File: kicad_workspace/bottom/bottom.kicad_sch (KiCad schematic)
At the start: 64 parts, among them J1 Battery connector, J2 Battery connector, M1 N20_MOTOR_EXTENDED_SHAFT, M2 N20_MOTOR_EXTENDED_SHAFT, U1 DRV8833PWP, U12 ACS712-5A, U13 ACS712-5A, U3 STM32F303RETx, U4 BNO055, Y1 32.768kHz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

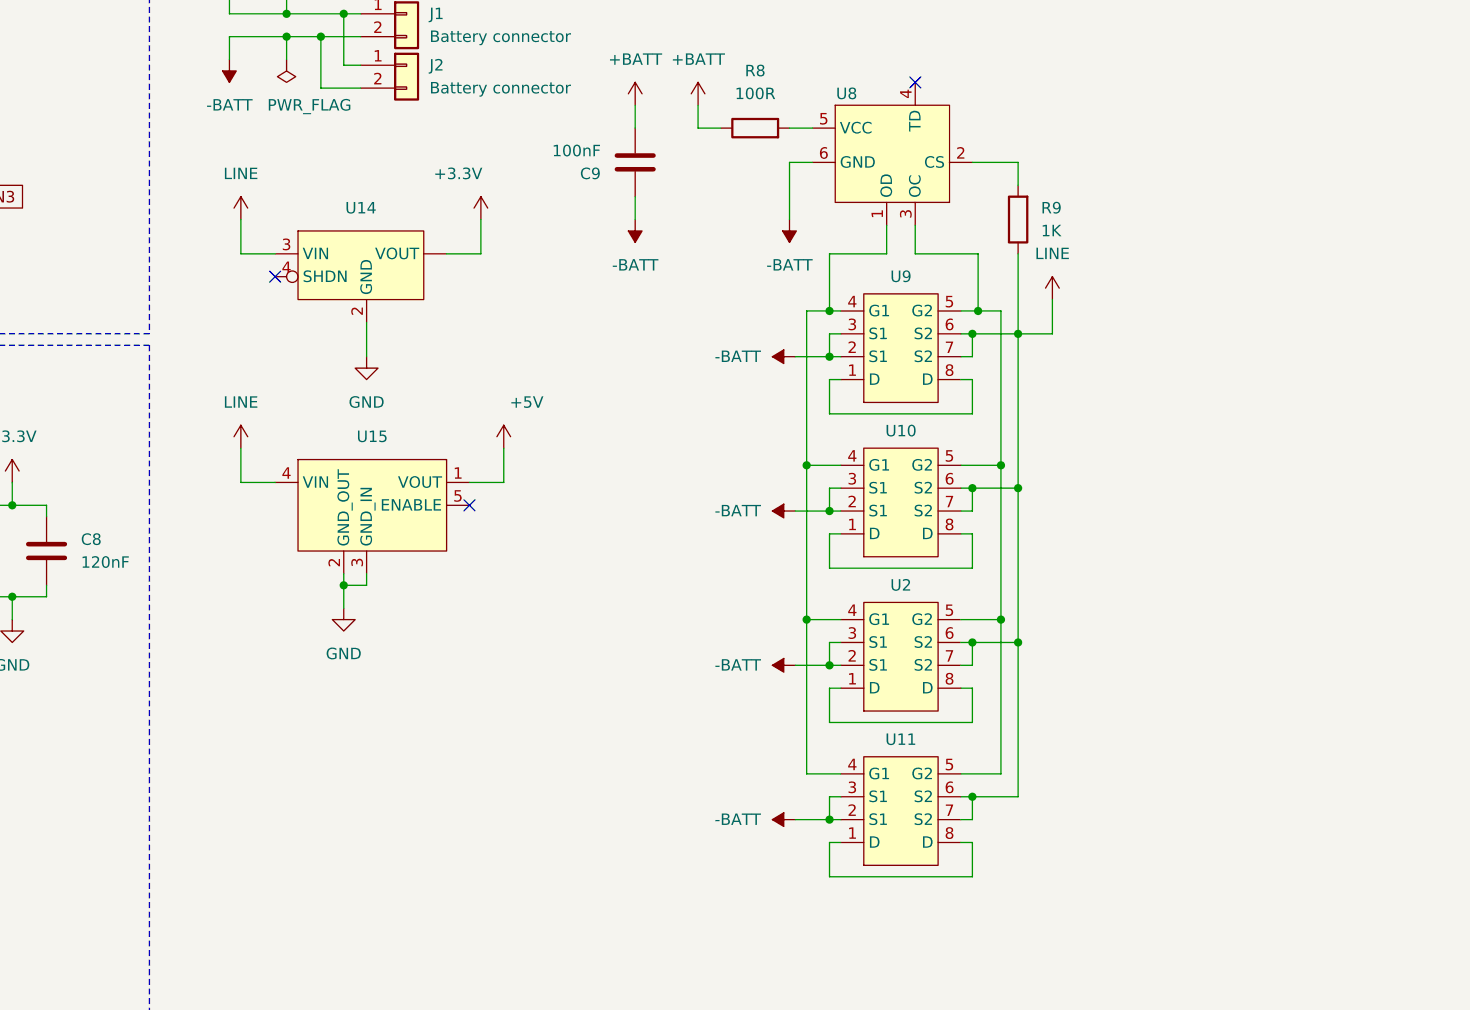
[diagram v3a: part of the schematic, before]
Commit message: add batt_prot symbol. clean schematic
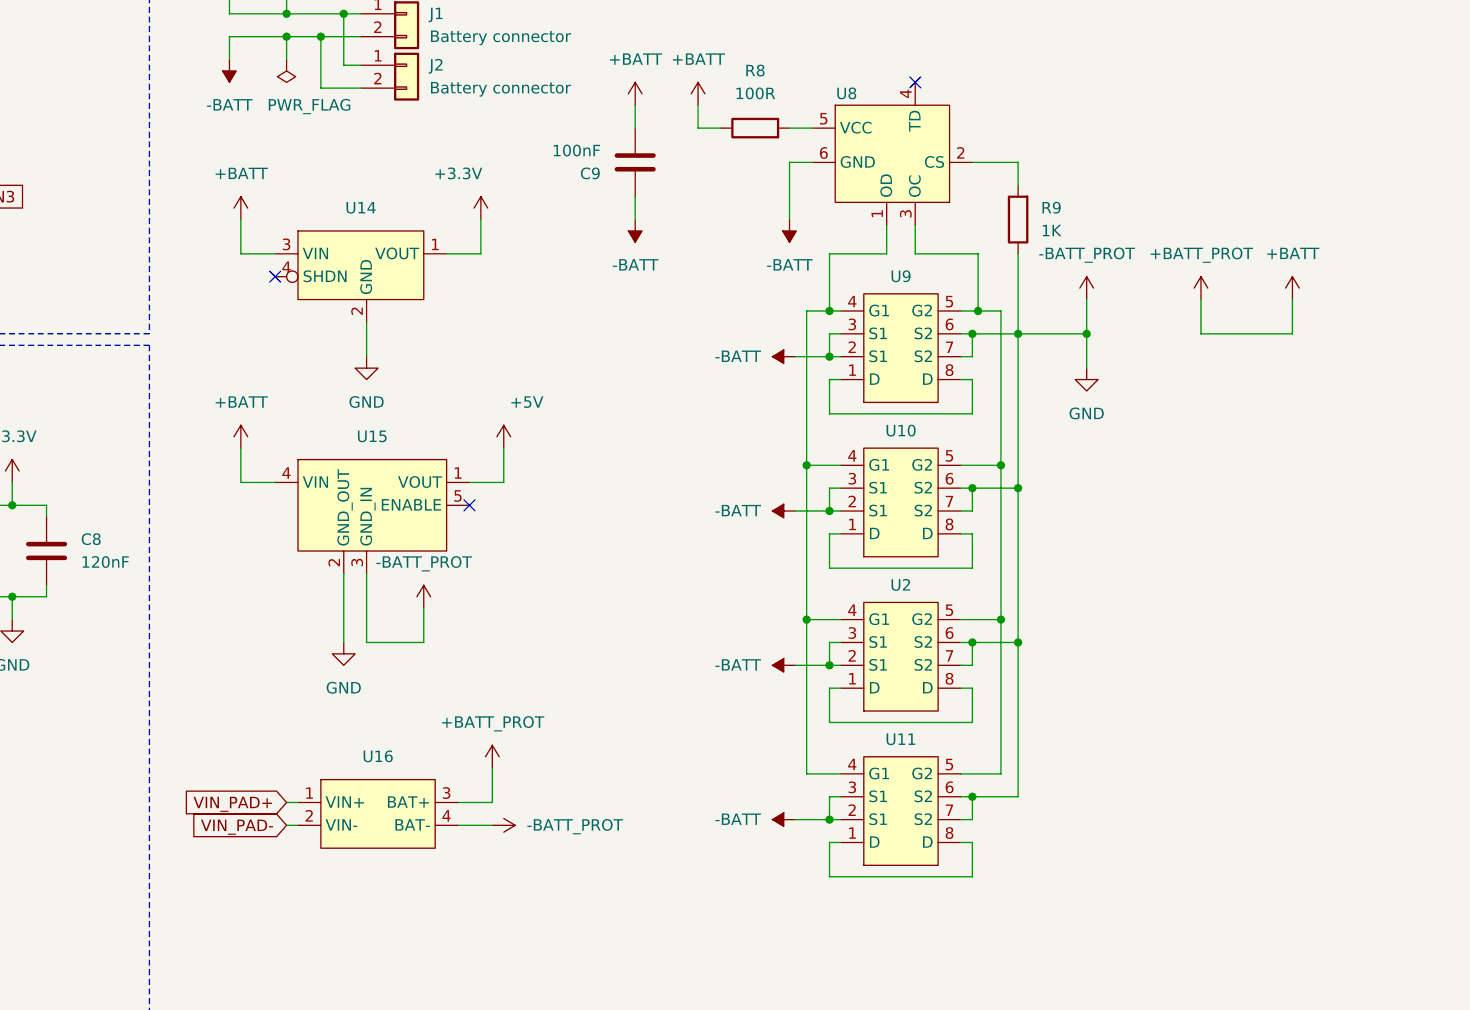
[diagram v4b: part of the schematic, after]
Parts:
- added U16: ~, pololu:TP5100, symbol pololu:TP5100
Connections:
- net +3.3V: now also U14.1 (VOUT); no longer U14. (VOUT)
- net +BATT: now also U14.3 (VIN), U15.4 (VIN), U16.3 (BAT+)
- net GND renamed -BATT_PROT
- net -BATT_PROT: now also R9.1, U10.6 (S2), U10.7 (S2), U11.6 (S2), U11.7 (S2), U2.6 (S2), U2.7 (S2), U9.6 (S2), U9.7 (S2), U16.4 (BAT-)
- removed net LINE: R9.1, U10.6 (S2), U10.7 (S2), U11.6 (S2), U11.7 (S2), U14.3 (VIN), U15.4 (VIN), U2.6 (S2), U2.7 (S2), U9.6 (S2), U9.7 (S2)
- new net VIN_PAD+: U16.1 (VIN+)
- new net VIN_PAD-: U16.2 (VIN-)

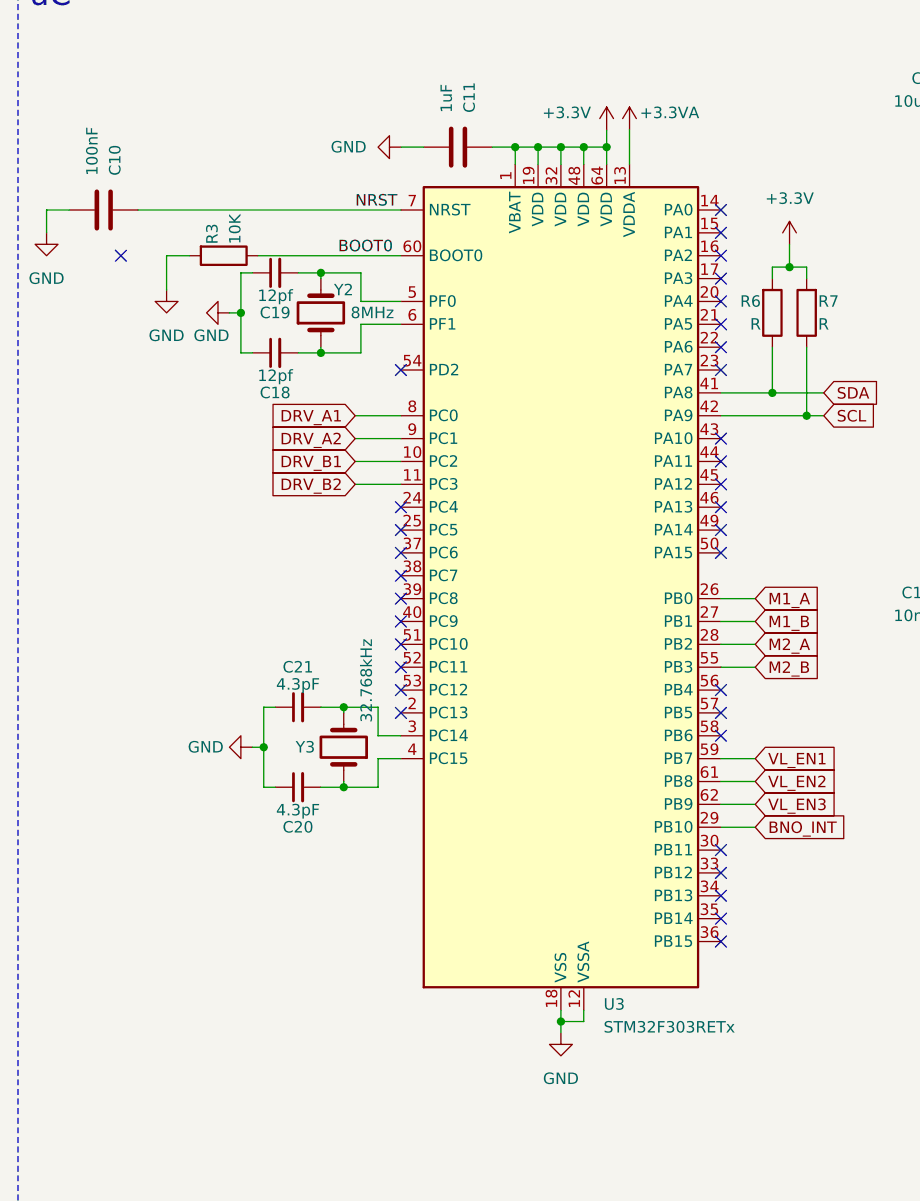
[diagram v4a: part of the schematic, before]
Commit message: changed uC to STM32H7A3RIT6
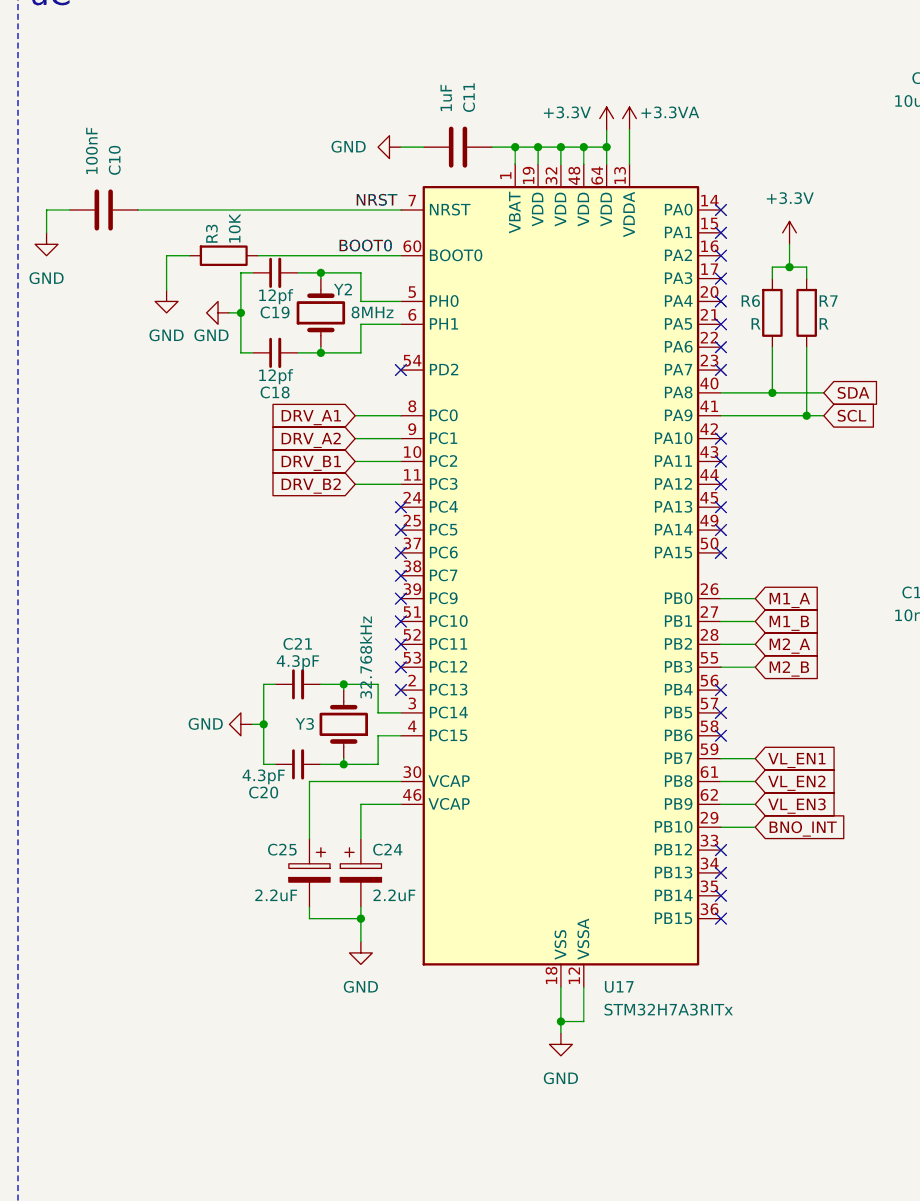
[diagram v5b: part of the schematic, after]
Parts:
- removed U3: STM32F303RETx, Package_QFP:LQFP-64_10x10mm_P0.5mm, symbol MCU_ST_STM32F3:STM32F303RETx
- added C24, C25: 2.2uF, Capacitor_SMD:CP_Elec_4x3, symbol Device:C_Polarized
- added U17: STM32H7A3RITx, Package_QFP:LQFP-64_10x10mm_P0.5mm, symbol MCU_ST_STM32H7:STM32H7A3RITx
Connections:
- net +3.3V: now also U17.1 (VBAT), U17.19 (VDD), U17.32 (VDD), U17.48 (VDD), U17.64 (VDD)
- net +3.3VA: now also U17.13 (VDDA)
- net -BATT_PROT: now also C24.2, C25.2, U17.12 (VSSA), U17.18 (VSS), U17.31 (VSS), U17.47 (VSS), U17.63 (VSS)
- net BNO_INT: now also U17.29 (PB10)
- net BOOT0: now also U17.60 (BOOT0)
- net DRV_A1: now also U17.8 (PC0)
- net DRV_A2: now also U17.9 (PC1)
- net DRV_B1: now also U17.10 (PC2)
- net DRV_B2: now also U17.11 (PC3)
- net M1_A: now also U17.26 (PB0)
- net M1_B: now also U17.27 (PB1)
- net M2_A: now also U17.28 (PB2)
- net M2_B: now also U17.55 (PB3)
- net NRST: now also U17.7 (NRST)
- net SCL: now also U17.41 (PA9)
- net SDA: now also U17.40 (PA8)
- net VL_EN1: now also U17.59 (PB7)
- net VL_EN2: now also U17.61 (PB8)
- net VL_EN3: now also U17.62 (PB9)
- net at C21.2, Y3.2: now also U17.3 (PC14)
- net at C18.2, Y2.1: now also U17.6 (PH1)
- net at C20.2, Y3.1: now also U17.4 (PC15)
- net at C19.2, Y2.2: now also U17.5 (PH0)
- new net: C25.1, U17.30 (VCAP)
- new net: C24.1, U17.46 (VCAP)
- no-connect marks 43 -> 40
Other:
- moved on the sheet: C20, C21, Y3

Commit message: changed tp5100 footprint to smd. add wiring for li-ion protection and charging
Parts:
- removed C20, C21: 4.3pF, Capacitor_SMD:C_0805_2012Metric, symbol Device:C_Small
- removed C24, C25: 2.2uF, Capacitor_SMD:CP_Elec_4x3, symbol Device:C_Polarized
- removed Y3: 32.768kHz, Crystal:Crystal_SMD_MicroCrystal_CM9V-T1A-2Pin_1.6x1.0mm, symbol Device:Crystal
- added C24, C25: 2.2uF, Capacitor_SMD:C_0805_2012Metric, symbol Device:C
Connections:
- net -BATT_PROT: now also C24.2, C25.2
- net BNO_INT: no longer U17.29 (PB10)
- net DRV_A1: no longer U17.8 (PC0)
- net DRV_A2: no longer U17.9 (PC1)
- net DRV_B1: no longer U17.10 (PC2)
- net DRV_B2: no longer U17.11 (PC3)
- net IP_MOTOR_A+: now also U13.3 (IP-), U13.4 (IP-); no longer U13.1 (IP+), U13.2 (IP+)
- net IP_MOTOR_A-: now also U13.1 (IP+), U13.2 (IP+); no longer U13.3 (IP-), U13.4 (IP-)
- net M1_A: no longer U17.26 (PB0)
- net M1_B: no longer U17.27 (PB1)
- net M2_A: no longer U17.28 (PB2)
- net M2_B: no longer U17.55 (PB3)
- net VL_EN1: no longer U17.59 (PB7)
- net VL_EN2: no longer U17.61 (PB8)
- net VL_EN3: no longer U17.62 (PB9)
- net at U17.30 (VCAP): now also C24.1
- net at U17.46 (VCAP): now also C25.1
- no-connect marks 40 -> 54

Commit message: wired motors
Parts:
- added C20, C21: 2.2uF, Capacitor_SMD:C_0805_2012Metric, symbol Device:C
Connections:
- net +3.3V: no longer U1.14 (VINT)
- net +5V: now also C20.1, C21.1
- net -BATT_PROT: now also C21.2
- net DRV_SLEEP: now reaches U1.1 (nSLEEP)
- net MOTOR_A-: now reaches M1.6 (M1), U1.2 (AOUT1)
- net MOTOR_B-: now reaches M2.6 (M1), U1.7 (BOUT1)
- net DRV_FAULT: now reaches U1.8 (nFAULT)
- net SWDIO: now reaches U17.45 (PA13)
- net SWCLK: now reaches U17.49 (PA14)
- net SWO: now reaches U17.55 (PB3)
- net VL_IRQ2: now reaches U6.5 (GPIO1)
- net VL_IRQ1: now reaches U5.5 (GPIO1)
- net VL_IRQ3: now reaches U7.5 (GPIO1)
- new net: C20.2, U1.14 (VINT)
- no-connect marks 54 -> 46
